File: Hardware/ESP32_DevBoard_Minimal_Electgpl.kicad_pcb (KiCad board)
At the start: 4 copper layers, 22.9 x 58.5 mm, 38 parts, among them J1 U254-051T-4BH83-F1S, J2 Conn_01x22_Pin, J3 Conn_01x22_Pin, SW1 SW_Push, U1 MCP1826S-3302E/DB, U2 ESP32-S3, U3 W25Q64JVSSIQ, Y1 R940000096

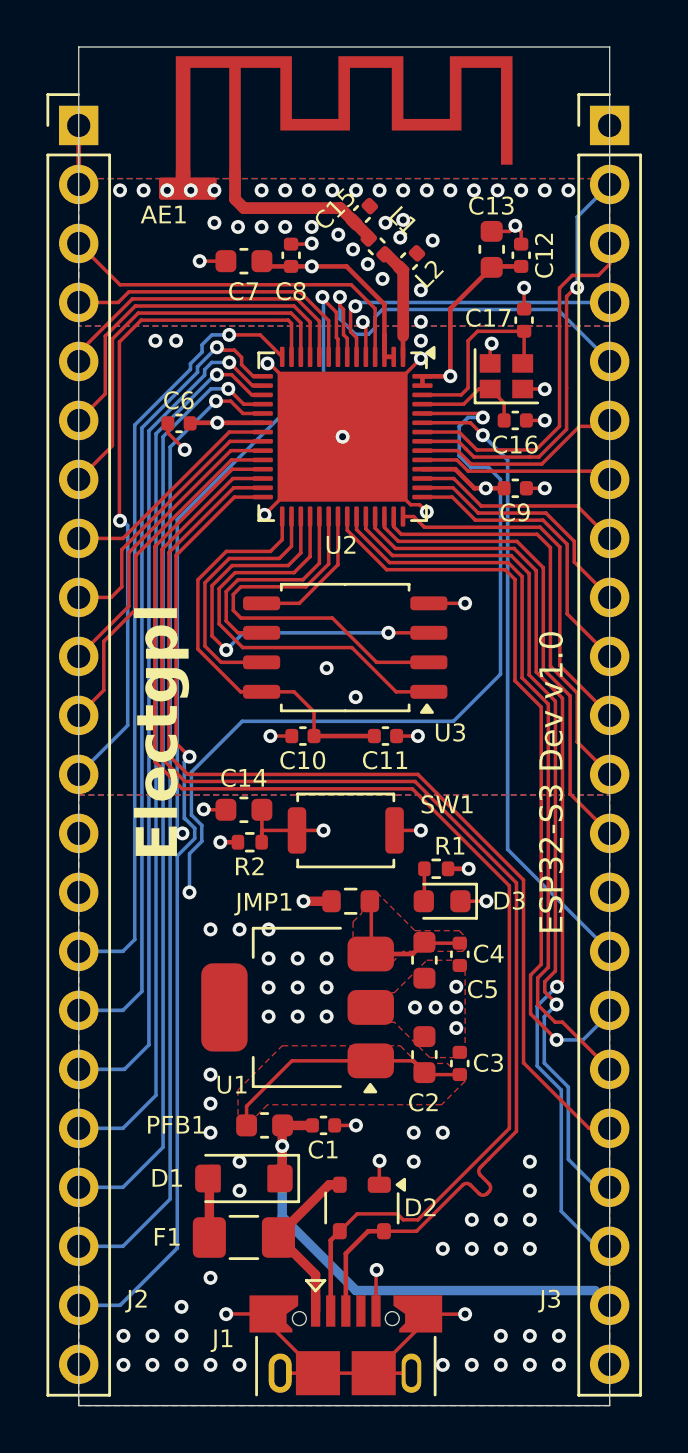
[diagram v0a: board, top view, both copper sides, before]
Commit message: feather format and DRC check
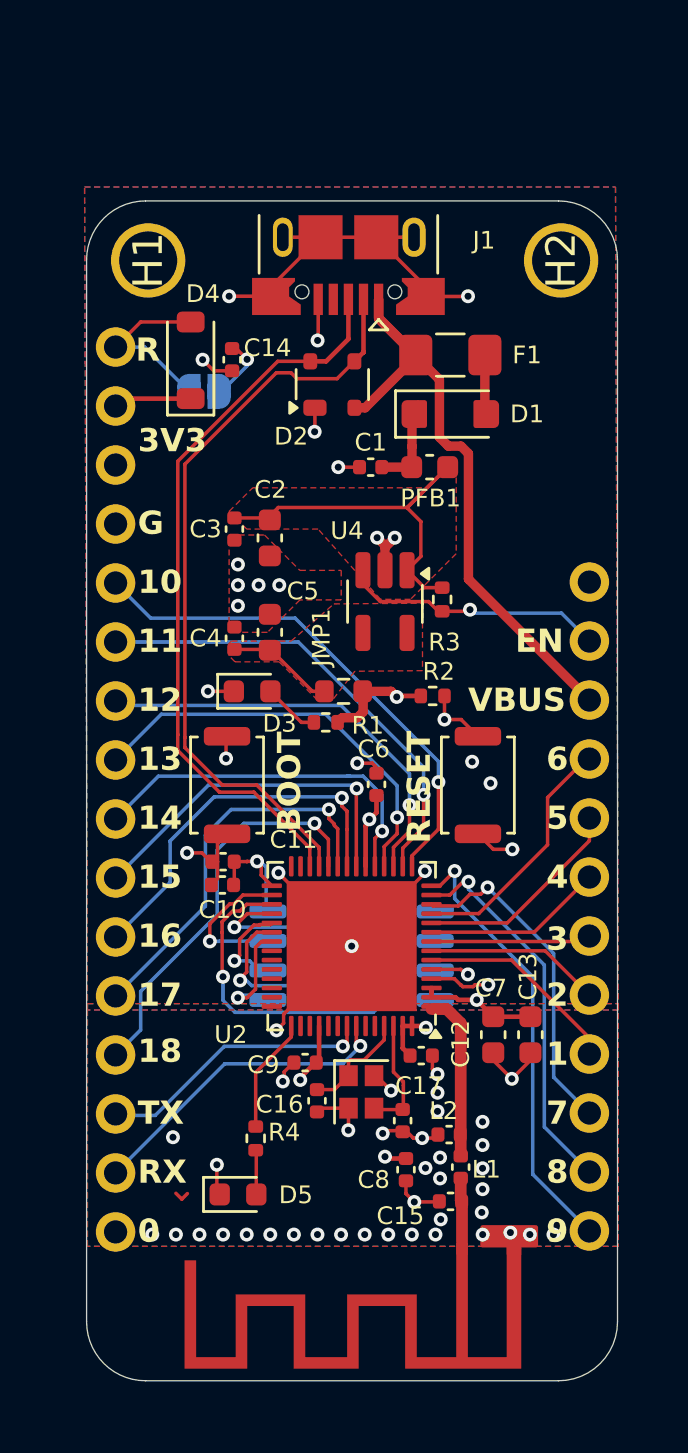
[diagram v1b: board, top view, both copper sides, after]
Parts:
- removed G***: LOGO, EXO_LIB_GIT:Recognized Component very small
- removed G***: LOGO, EXO_LIB_GIT:Warning_3mm
- removed J2, J3: Conn_01x22_Pin, Connector_PinHeader_2.54mm:PinHeader_1x22_P2.54mm_Vertical
- removed U1: MCP1826S-3302E/DB, Package_TO_SOT_SMD:SOT-223
- added D4: DS310W, Diode_SMD:D_SOD-123, F.Cu at (141.5, 84.9)
- added D5: LED, LED_SMD:LED_0603_1608Metric, F.Cu at (143.5, 120.8)
- added H1: MountingHole, , F.Cu at (139.6, 80.6)
- added H2: MountingHole, , F.Cu at (157.4, 80.6)
- added JP1: Conn_01x16_Pin, Connector_PinHeader_2.54mm:PinHeader_1x16_P2.54mm_Vertical, B.Cu at (138.2, 122.4)
- added JP2: Conn_01x12_Pin, Connector_PinHeader_2.54mm:PinHeader_1x12_P2.54mm_Vertical, B.Cu at (158.6, 94.4)
- added JP3: SolderJumper_2_Open, Jumper:SolderJumper-2_P1.3mm_Open_RoundedPad1.0x1.5mm, B.Cu at (142.1, 86.2)
- added R3: 10k, Resistor_SMD:R_0402_1005Metric, F.Cu at (152.3, 95.2)
- added R4: 10k, Resistor_SMD:R_0402_1005Metric, F.Cu at (144.3, 118.4)
- added SW2: SW_Push, Button_Switch_SMD:SW_Push_SPST_NO_Alps_SKRK, F.Cu at (143.0, 103.2)
- added U4: AP2112/RT9080-3.3, Package_TO_SOT_SMD:SOT-23-5_HandSoldering, F.Cu at (149.8, 95.3)
- AE1: value Antenna_Shield -> MIFA
- C14: value 10u -> 100n; footprint Capacitor_SMD:C_0603_1608Metric -> Capacitor_SMD:C_0402_1005Metric
- U3: moved to B.Cu
- moved J1 48.1 mm to (148.3, 80.0), turned to 180 degrees
- moved AE1 47.2 mm to (153.0, 123.1), turned to 180 degrees
- moved C15 42.7 mm to (152.7, 121.1), turned to 180 degrees
- moved L1 39.8 mm to (153.1, 119.6), turned to 90 degrees
- moved C8 39.7 mm to (150.7, 119.7), turned to -90 degrees
- moved F1 39.0 mm to (152.7, 84.6), turned to 0 degrees
- moved L2 37.6 mm to (152.6, 118.2), turned to 180 degrees
- moved D2 35.5 mm to (147.6, 85.9), turned to 90 degrees
- moved C7 35.0 mm to (154.5, 113.9), turned to -90 degrees
- moved C17 34.9 mm to (150.6, 117.6), turned to -90 degrees
- moved C12 34.7 mm to (151.4, 114.8), turned to 0 degrees
- moved D1 34.1 mm to (152.7, 87.2), turned to 0 degrees
- moved C13 33.9 mm to (156.1, 113.9), turned to -90 degrees
- moved Y1 31.4 mm to (148.8, 116.4), turned to -90 degrees
- moved C16 30.5 mm to (146.9, 116.7), turned to -90 degrees
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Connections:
- net Net-(U1-VO) renamed /REGUOT
- C14 pad 1: CHIP_PU -> Net-(JP3-A)
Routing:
- net GPIO21: track 44.2 -> 0.00 mm
- net GPIO46: track 41.1 -> 0.00 mm, vias 2 -> 0
- net GPIO26: track 40.7 -> 0.00 mm, vias 1 -> 0
- net GPIO34: track 39.3 -> 0.00 mm, vias 1 -> 0
- net GPIO33: track 36.8 -> 0.00 mm, vias 1 -> 0
- net GPIO48: track 32.5 -> 0.00 mm, vias 1 -> 0
- net GPIO47: track 31.9 -> 0.00 mm
- net GPIO45: track 27.3 -> 0.00 mm, vias 1 -> 0
- net GPIO14: track 42.2 -> 15.9 mm
- net GPIO3: track 33.1 -> 6.90 mm, vias 2 -> 0
- net +3.3V: track 98.6 -> 72.8 mm, vias 7 -> 6
- net D_P: track 56.3 -> 31.9 mm
- net D_M: track 56.1 -> 32.7 mm
- net GPIO13: track 40.4 -> 18.3 mm
- net GPIO35: track 20.7 -> 0.00 mm
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- added copper zone on In2.Cu, net +3.3V
- removed copper zone on In2.Cu, net GND
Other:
- board size 22.9 x 58.5 mm -> 22.9 x 50.8 mm
- board text added: "0"
- board text added: "1"
- board text added: "10"
- board text added: "11"
- board text added: "12"
- board text added: "13"
- board text added: "14"
- board text added: "15"
- board text added: "16"
- board text added: "17"
- board text added: "18"
- board text added: "2"
- board text added: "3"
- board text added: "4"
- board text added: "5"
- board text added: "6"
- board text added: "7"
- board text added: "8"
- board text added: "9"
- board text added: "BOOT"
- board text added: "EN"
- board text added: "G"
- board text added: "R"
- board text added: "RESET"
- board text added: "RX"
- board text added: "S3 v1.01"
- board text added: "TX"
- board text added: "VBUS"
- board text removed: "1525"
- board text removed: "94V-0 E479892 JLC-2"
- board text removed: "CHIP_PU"
- board text removed: "DESIGN ARGENTINA"
- board text removed: "ESP32-S3 Dev v1.0"
- board text removed: "ESP32S3 Dev v1.0"
- board text removed: "Electgpl"
- board text removed: "GND"
- board text removed: "GPIO0"
- board text removed: "GPIO1"
- board text removed: "GPIO10"
- board text removed: "GPIO11"
- board text removed: "GPIO12"
- board text removed: "GPIO13"
- board text removed: "GPIO14"
- board text removed: "GPIO15"
- board text removed: "GPIO16"
- board text removed: "GPIO17"
- board text removed: "GPIO18"
- board text removed: "GPIO2"
- board text removed: "GPIO21"
- board text removed: "GPIO26"
- board text removed: "GPIO3"
- board text removed: "GPIO33"
- board text removed: "GPIO34"
- board text removed: "GPIO35"
- board text removed: "GPIO36"
- board text removed: "GPIO37"
- board text removed: "GPIO38"
- board text removed: "GPIO39"
- board text removed: "GPIO4"
- board text removed: "GPIO40"
- board text removed: "GPIO41"
- board text removed: "GPIO42"
- board text removed: "GPIO45"
- board text removed: "GPIO46"
- board text removed: "GPIO47"
- board text removed: "GPIO48"
- board text removed: "GPIO5"
- board text removed: "GPIO6"
- board text removed: "GPIO7"
- board text removed: "GPIO8"
- board text removed: "GPIO9"
- board text removed: "RAW"
- board text removed: "RAW Vmax: 6V"
- board text removed: "RXD"
- board text removed: "TXD"

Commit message: add u.FL antenna connector
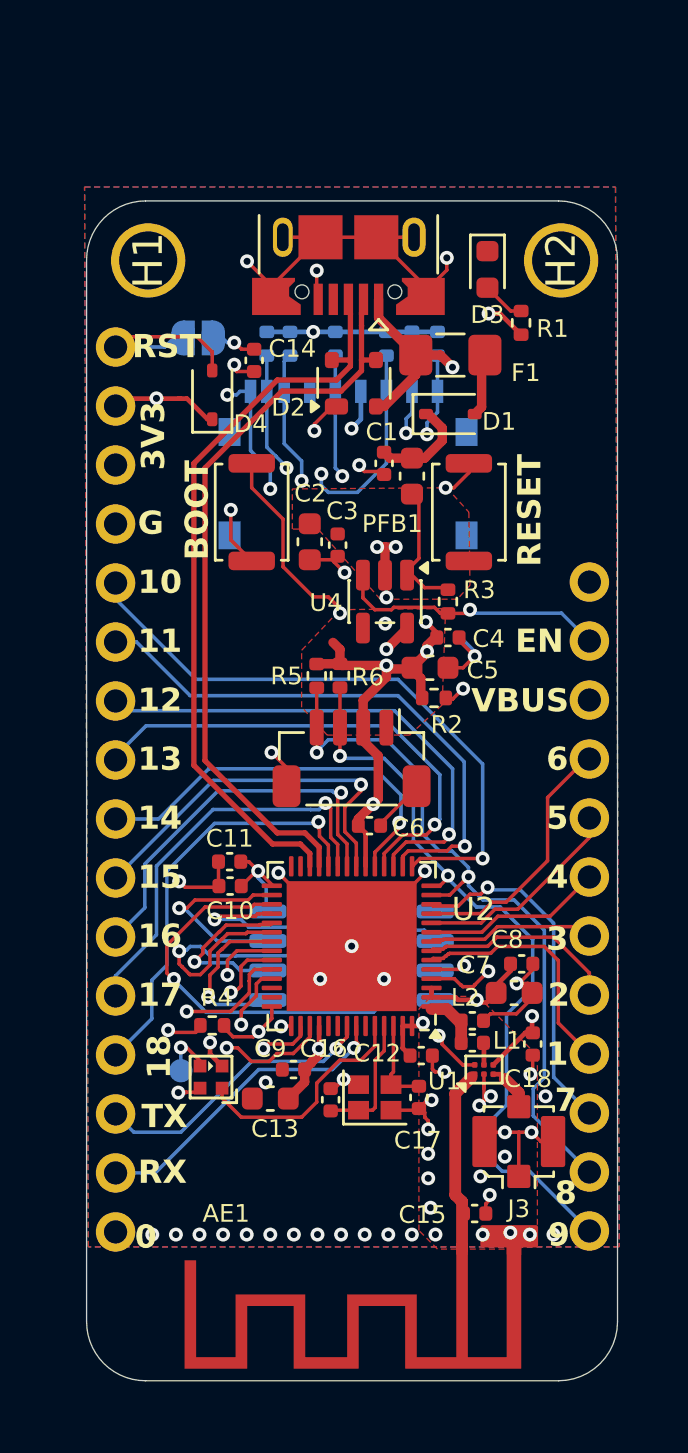
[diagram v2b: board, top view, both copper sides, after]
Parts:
- removed D5: LED, LED_SMD:LED_0603_1608Metric
- removed JMP1: 0R, Resistor_SMD:R_0603_1608Metric
- added C18: 100n, Capacitor_SMD:C_0402_1005Metric, F.Cu at (156.2, 114.3)
- added CONN1: QUICC, Connector_JST:JST_SH_BM04B-SRSS-TB_1x04-1MP_P1.00mm_Vertical, F.Cu at (148.4, 102.0)
- added J2: microSD_Friction, Library:TF-SMD_TF-018, B.Cu at (148.2, 89.3)
- added J3: Conn_Coaxial_Small, Connector_Coaxial:U.FL_Molex_MCRF_73412-0110_Vertical, F.Cu at (155.6, 118.5)
- added LED1: WS2812B_SK6805_1515, Library:LED-SMD_4P-L1.5-W1.5-BL, F.Cu at (142.3, 115.7)
- added R10: 10k, Resistor_SMD:R_0402_1005Metric, B.Cu at (152.1, 84.2)
- added R11: 10k, Resistor_SMD:R_0402_1005Metric, B.Cu at (151.0, 84.1)
- added R12: 10k, Resistor_SMD:R_0402_1005Metric, B.Cu at (144.8, 84.2)
- added R5: 10k, Resistor_SMD:R_0402_1005Metric, F.Cu at (146.9, 98.5)
- added R6: 10k, Resistor_SMD:R_0402_1005Metric, F.Cu at (147.9, 98.4)
- added R7: 10k, Resistor_SMD:R_0402_1005Metric, B.Cu at (149.9, 84.2)
- added R8: 10k, Resistor_SMD:R_0402_1005Metric, B.Cu at (147.7, 84.2)
- added R9: 10k, Resistor_SMD:R_0402_1005Metric, B.Cu at (145.8, 84.2)
- added TP1: TestPoint_Small, TestPoint:TestPoint_Pad_D1.0mm, B.Cu at (141.1, 115.5)
- added U1: BGS12WN6E6327, Package_LGA:Infineon_PG-TSNP-6-10_0.7x1.1mm_0.7x1.1mm_P0.4mm, F.Cu at (154.1, 115.4)
- D1, D4: value DS310W -> BAT60A; footprint Diode_SMD:D_SOD-123 -> Diode_SMD:D_SOD-323
- U4: value AP2112/RT9080-3.3 -> AP2112K-3.3TRG1; footprint Package_TO_SOT_SMD:SOT-23-5_HandSoldering -> Package_TO_SOT_SMD:SOT-23-5
- moved D3 20.8 mm to (154.2, 81.0), turned to -90 degrees
- moved R1 19.1 mm to (155.7, 83.2), turned to 90 degrees
- moved SW2 11.8 mm to (144.1, 91.4)
- moved SW1 11.8 mm to (153.4, 91.4)
- moved C13 11.5 mm to (144.9, 116.7), turned to 180 degrees
- moved C8 10.2 mm to (155.7, 110.8), turned to 0 degrees
- moved C4 9.19 mm to (152.6, 96.8), turned to 0 degrees
- moved C5 7.06 mm to (151.8, 98.1), turned to 0 degrees
- moved L1 5.37 mm to (153.6, 114.2), turned to 180 degrees
- moved R4 5.21 mm to (142.4, 113.5), turned to 180 degrees
- moved L2 5.00 mm to (153.6, 113.3), turned to 0 degrees
- moved C3 4.50 mm to (147.8, 92.8)
- moved JP3 2.31 mm to (141.8, 83.9)
- moved C7 2.01 mm to (155.4, 112.1), turned to 0 degrees
- moved C6 1.80 mm to (149.2, 104.9), turned to 0 degrees
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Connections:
- net D_M renamed USBD_N
- net D_P renamed USBD_P
- net Net-(U4-IN) renamed /VIN
- C4 pad 1: /REGUOT -> +3.3V
- C5 pad 1: /REGUOT -> +3.3V
- L1 pad 1: Net-(AE1-A) -> Net-(U1-RFIN)
- R4 pad 1: GPIO38 -> GPIO37
- R4 pad 2: Net-(D5-A) -> GND
- U4 pad 5: /REGUOT -> +3.3V
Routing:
- net +3.3V: track 72.8 -> 127.6 mm, vias 6 -> 15
- net GPIO33: track 0.00 -> 41.1 mm, vias 0 -> 2
- net GPIO47: track 0.00 -> 38.7 mm, vias 0 -> 2
- net GPIO34: track 0.00 -> 37.4 mm, vias 0 -> 2
- net GPIO40: track 0.00 -> 37.2 mm, vias 0 -> 2
- net GPIO39: track 0.00 -> 35.9 mm, vias 0 -> 2
- net GPIO48: track 0.00 -> 30.8 mm, vias 0 -> 3
- net GPIO38: track 4.96 -> 30.8 mm, vias 0 -> 2
- net GPIO0: track 37.2 -> 55.0 mm
- net GPIO8: track 16.5 -> 31.9 mm, vias 1 -> 2
- net GPIO9: track 19.2 -> 32.7 mm, vias 1 -> 2
- net GPIO37: track 0.00 -> 13.3 mm, vias 0 -> 2
- net /VIN: track 17.6 -> 5.67 mm
- net GPIO46: track 0.00 -> 9.96 mm
- net GND: track 62.5 -> 71.5 mm, vias 61 -> 56
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- added copper zone on F.Cu, net +3.3V
- removed copper zone on F.Cu, net /REGUOT
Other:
- board text added: "Controlled Impedance: JLC7628"
- board text added: "Inner Copper Weight: 0.5oz"
- board text added: "Material: TG155"
- board text added: "Outer Copper Weight: 1oz"
- board text added: "RST"
- board text added: "Thickness: 1.6mm"
- board text removed: "R"
